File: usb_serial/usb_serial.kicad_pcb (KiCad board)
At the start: 2 copper layers, 25.2 x 36 mm, 21 parts, among them P1 USB_OTG, P2 CONN_01X07, P3 CONN_01X07, Q1 S8050, Q2 S8050, U1 CH340G, X1 CRYSTAL_SMD

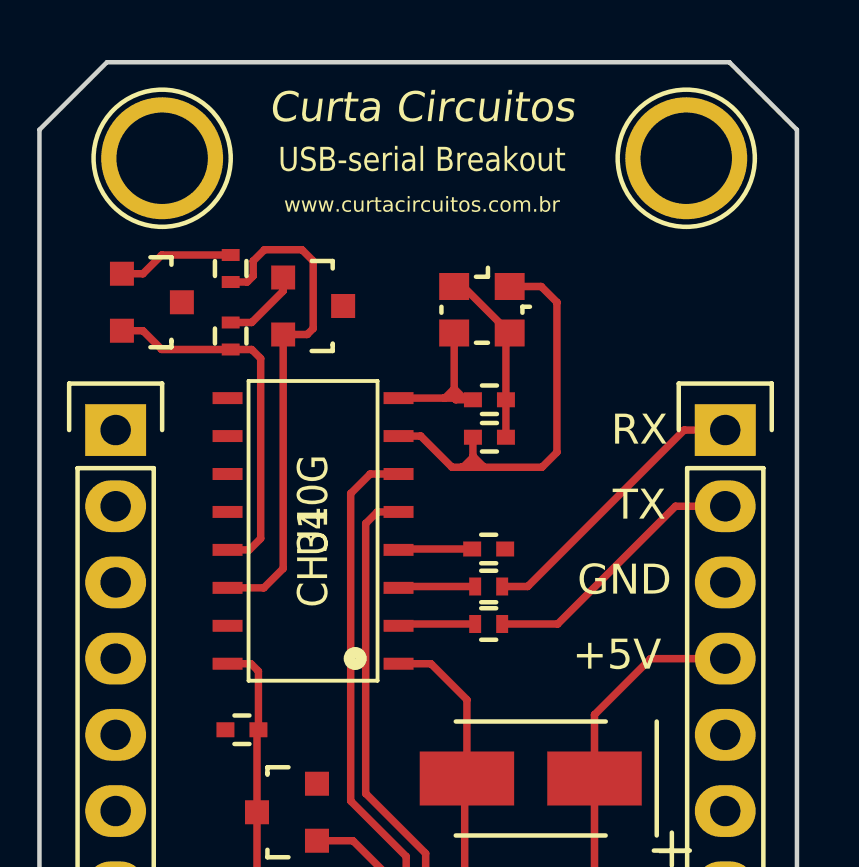
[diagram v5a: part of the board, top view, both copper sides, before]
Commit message: Reg. tensao finished, with renderings. Minor fixes in usb-serial
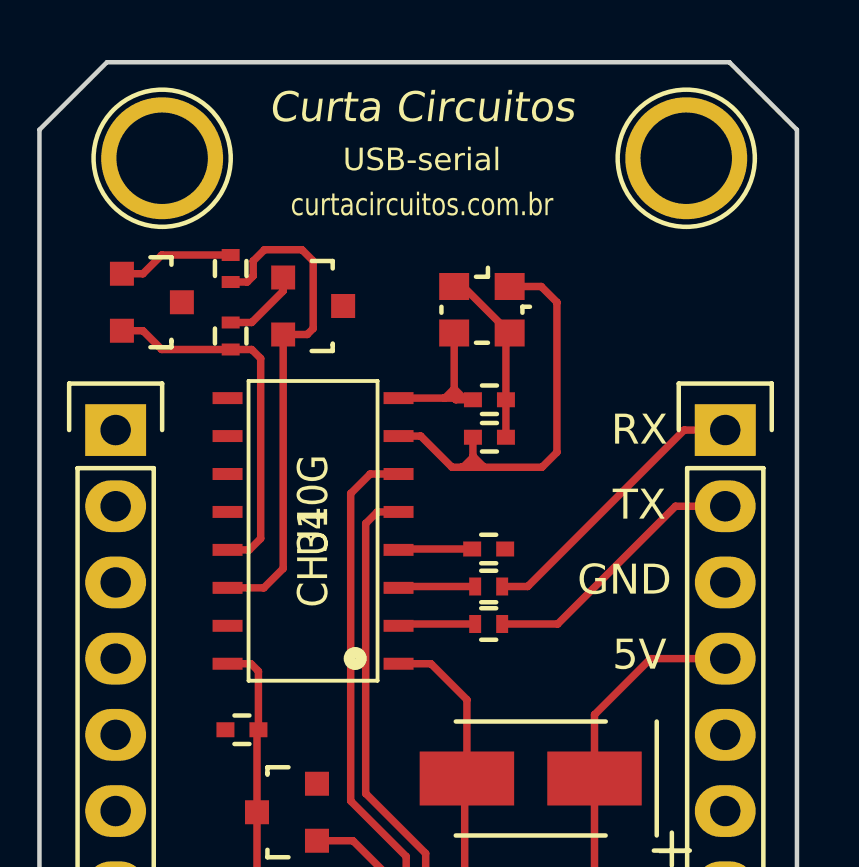
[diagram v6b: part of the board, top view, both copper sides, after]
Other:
- board text added: "5V"
- board text added: "USB-serial"
- board text added: "curtacircuitos.com.br"
- board text removed: "+5V"
- board text removed: "USB-serial Breakout"
- board text removed: "www.curtacircuitos.com.br"
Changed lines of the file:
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@@
     )
   )
-  (gr_text www.curtacircuitos.com.br (at 158.75 69.25) (layer F.SilkS)
-    (effects (font (size 0.5 0.5) (thickness 0.08)))
+  (gr_text curtacircuitos.com.br (at 158.75 69.25) (layer F.SilkS)
+    (effects (font (size 0.75 0.6) (thickness 0.125)))
   )
   (gr_line (start 148.25 64.5) (end 169 64.5) (angle 90) (layer Edge.Cuts) (width 0.15))
@@
     (effects (font (size 1 1) (thickness 0.2)))
   )
-  (gr_text +5V (at 165.25 84.25) (layer F.SilkS)
+  (gr_text 5V (at 166 84.25) (layer F.SilkS)
     (effects (font (size 1 1) (thickness 0.2)))
   )
-  (gr_text "USB-serial Breakout" (at 158.75 67.75) (layer F.SilkS)
-    (effects (font (size 0.8 0.7) (thickness 0.1)))
+  (gr_text USB-serial (at 158.75 67.75) (layer F.SilkS)
+    (effects (font (size 0.75 0.75) (thickness 0.15)))
   )
   (gr_text "Curta Circuitos" (at 158.75 66) (layer F.SilkS)
@@
   (segment (start 159.825 75.695) (end 159.88 75.75) (width 0.25) (layer F.Cu) (net 4))
   (segment (start 160.395 75.695) (end 160.45 75.75) (width 0.25) (layer F.Cu) (net 4))
-  (segment (start 164.50098 88.375) (end 164.50098 86.24902) (width 0.25) (layer F.Cu) (net 5) (status 400000))
-  (segment (start 166.37 84.38) (end 168.86 84.38) (width 0.25) (layer F.Cu) (net 5) (status 800000))
+  (segment (start 164.50098 88.375) (end 164.50098 86.24902) (width 0.25) (layer F.Cu) (net 5))
+  (segment (start 166.37 84.38) (end 168.86 84.38) (width 0.25) (layer F.Cu) (net 5))
   (segment (start 164.50098 86.24902) (end 166.37 84.38) (width 0.25) (layer F.Cu) (net 5))
   (segment (start 164.50098 88.375) (end 164.50098 98.49902) (width 0.25) (layer F.Cu) (net 5))
